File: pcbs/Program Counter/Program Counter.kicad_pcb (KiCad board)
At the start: 2 copper layers, 12 parts, among them J1001 Conn_02x20_Odd_Even, J1002 Conn_02x20_Odd_Even, U2001 74HC245, U2002 74HC245, U3001 74HC245, U3002 74HC245, U4001 74HC245, U4002 74HC245, U5001 74HC245, U5002 74HC245

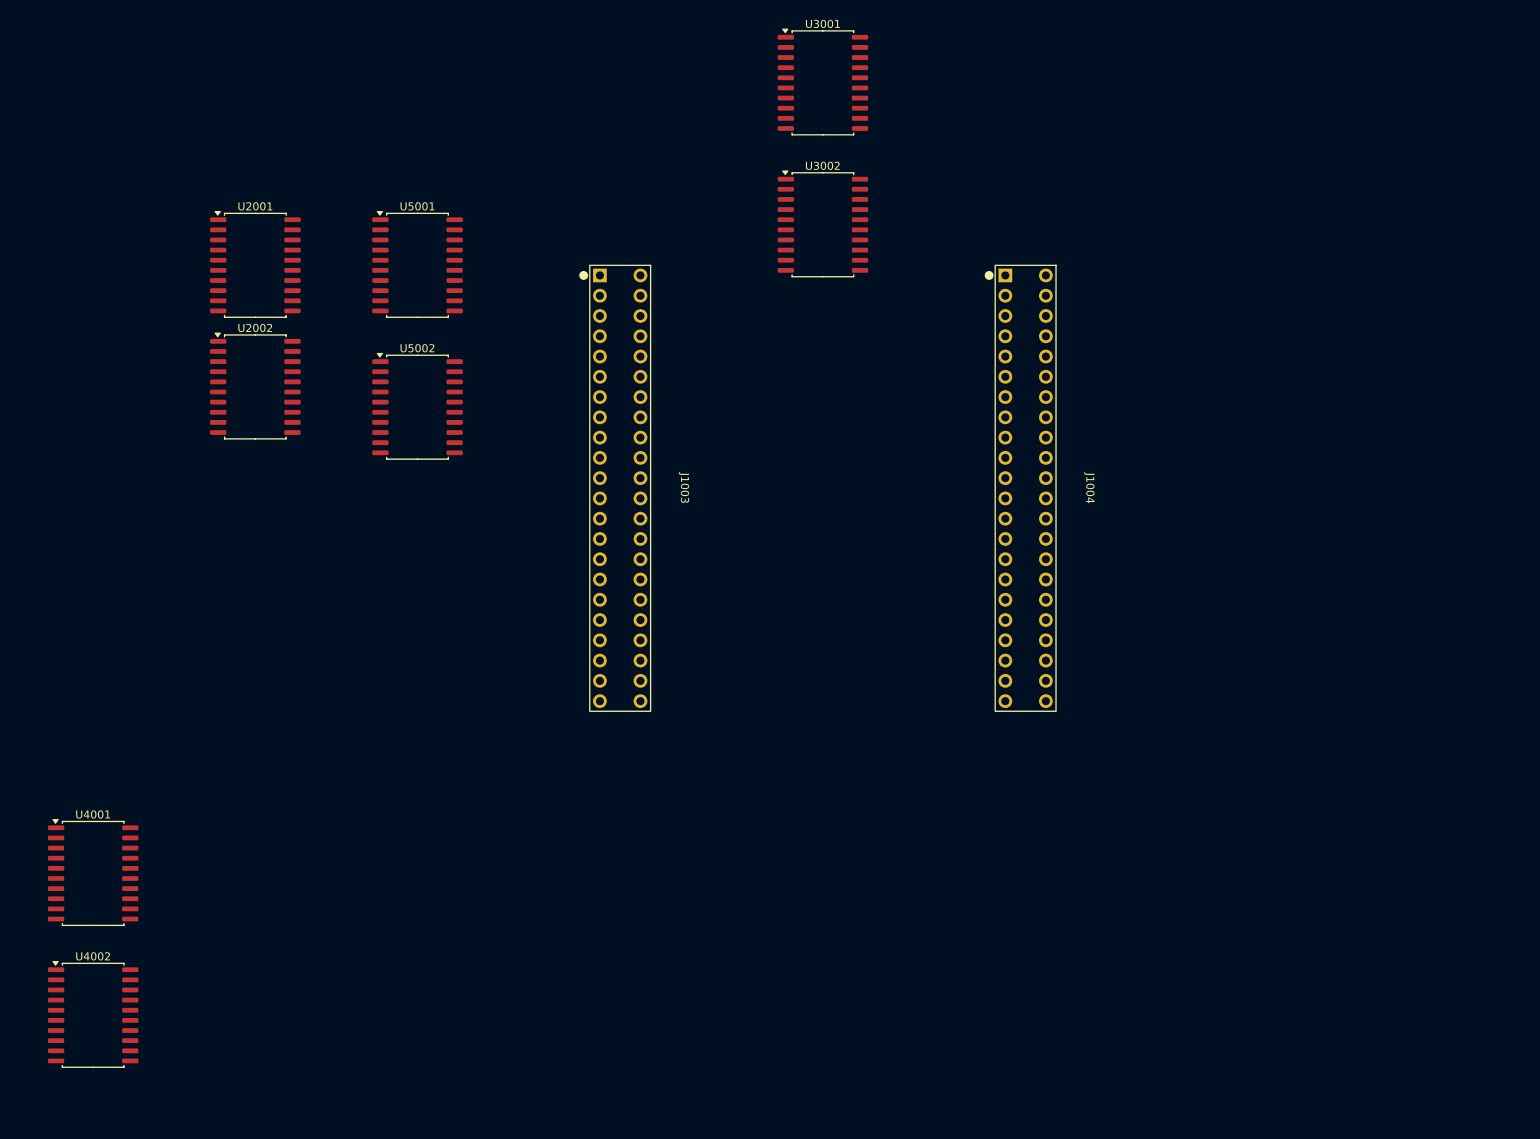
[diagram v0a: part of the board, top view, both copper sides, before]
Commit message: Some preliminary routing
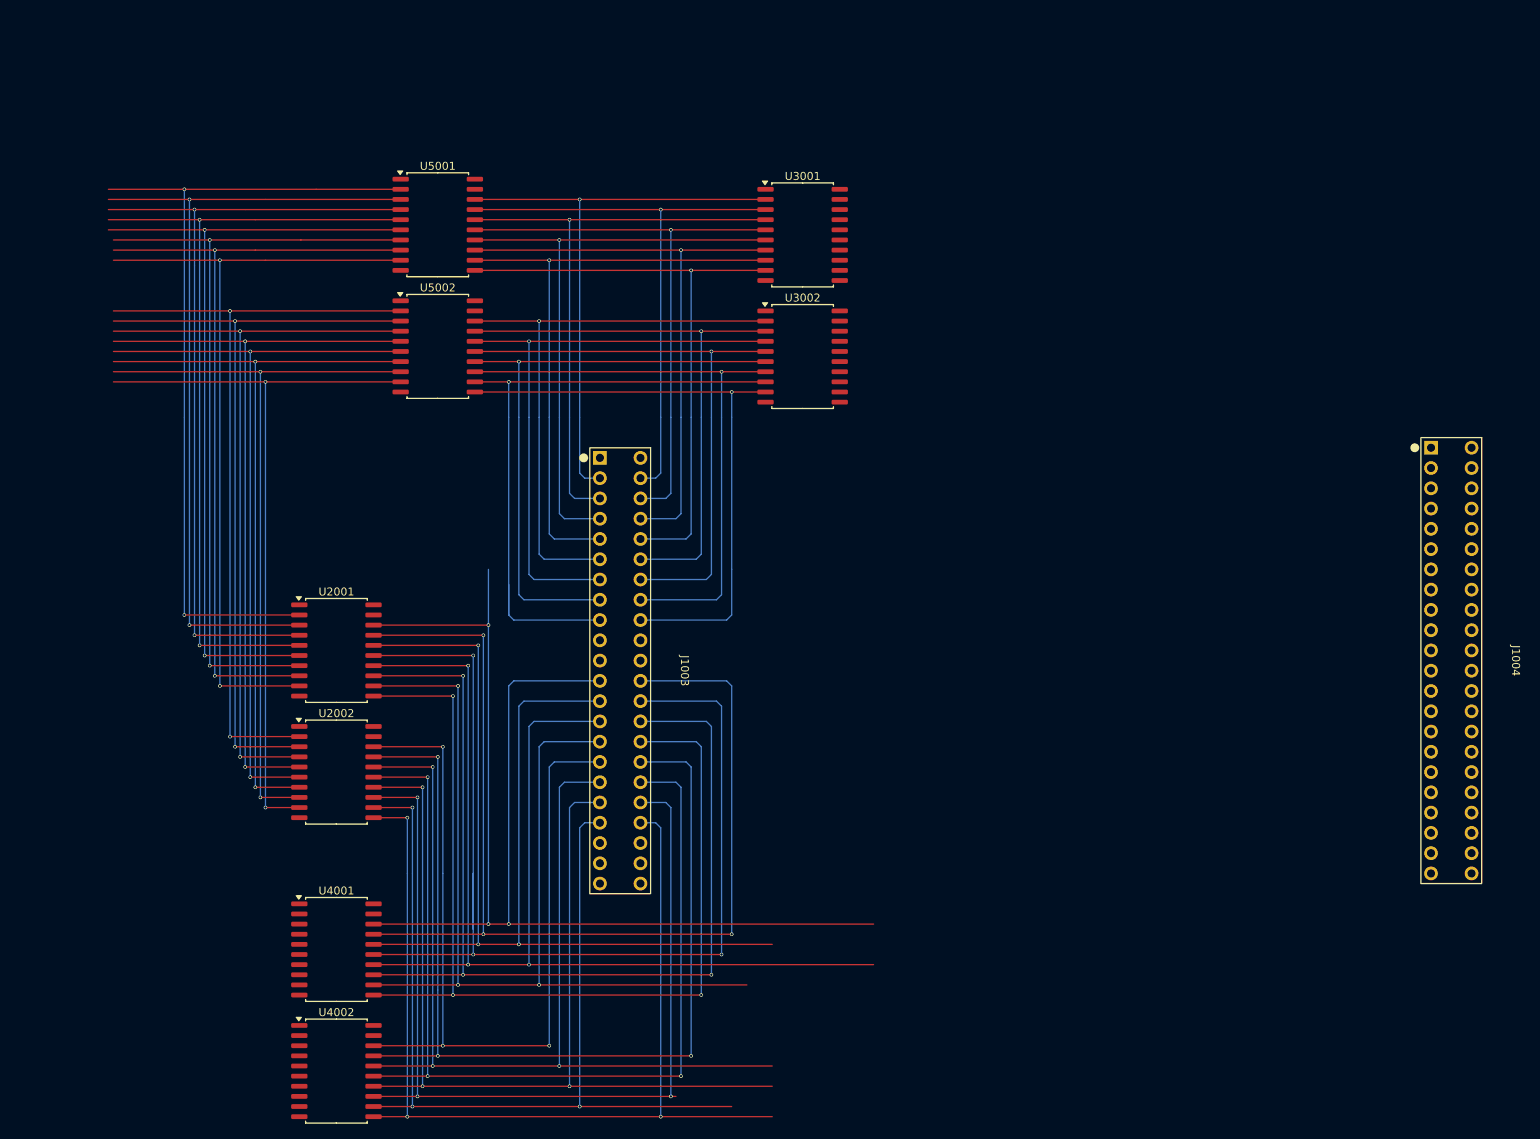
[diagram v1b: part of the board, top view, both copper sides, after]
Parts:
- moved J1004 57.5 mm to (231.1, 100.3)
- moved U2001 49.3 mm to (91.4, 99.1)
- moved U2002 49.3 mm to (91.4, 114.3)
- moved U4001 31.9 mm to (91.4, 136.5)
- moved U4002 31.3 mm to (91.4, 151.8)
- moved J1003 22.9 mm to (127.0, 101.6)
- moved U3001 19.2 mm to (149.9, 47.0)
- moved U3002 16.7 mm to (149.9, 62.2)
- moved U5002 8.03 mm to (104.1, 61.0)
- moved U5001 5.68 mm to (104.1, 45.7)
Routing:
- net /PC.Out0: track 0.00 -> 163.0 mm, vias 0 -> 3
- net /PC.Out4: track 0.00 -> 151.0 mm, vias 0 -> 3
- net /PC.Out3: track 0.00 -> 149.1 mm, vias 0 -> 3
- net /PC.Out2: track 0.00 -> 140.8 mm, vias 0 -> 3
- net /PC.Out1: track 0.00 -> 138.9 mm, vias 0 -> 3
- net /PC.Out10: track 0.00 -> 135.1 mm, vias 0 -> 3
- net /PC.Out6: track 0.00 -> 132.6 mm, vias 0 -> 3
- net /PC.Out12: track 0.00 -> 132.6 mm, vias 0 -> 3
- net /PC.Out5: track 0.00 -> 131.3 mm, vias 0 -> 3
- net /PC.Out15: track 0.00 -> 130.7 mm, vias 0 -> 3
- net /PC.Out9: track 0.00 -> 128.1 mm, vias 0 -> 3
- net /PC.Out7: track 0.00 -> 127.5 mm, vias 0 -> 3
- net /PC.Out14: track 0.00 -> 124.9 mm, vias 0 -> 3
- net /PC.Out11: track 0.00 -> 124.3 mm, vias 0 -> 3
- net /PC.Out13: track 0.00 -> 121.1 mm, vias 0 -> 3
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
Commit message: Thinking about more circuitry
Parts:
- added C6001: 100n, Capacitor_SMD:C_0603_1608Metric, F.Cu at (93.6, 191.5)
- added D6001: Blue, LED_SMD:LED_0603_1608Metric, F.Cu at (112.4, 184.2)
- added D6002: Blue, LED_SMD:LED_0603_1608Metric, F.Cu at (114.3, 198.2)
- added D6003: Blue, LED_SMD:LED_0603_1608Metric, F.Cu at (114.3, 200.8)
- added D6004: Blue, LED_SMD:LED_0603_1608Metric, F.Cu at (114.3, 203.3)
- added D6005: Blue, LED_SMD:LED_0603_1608Metric, F.Cu at (114.3, 205.9)
- added D6006: Blue, LED_SMD:LED_0603_1608Metric, F.Cu at (114.3, 208.5)
- added D6007: Blue, LED_SMD:LED_0603_1608Metric, F.Cu at (114.3, 211.1)
- added D6008: Blue, LED_SMD:LED_0603_1608Metric, F.Cu at (114.3, 213.7)
- added D6009: Blue, LED_SMD:LED_0603_1608Metric, F.Cu at (114.3, 216.3)
- added R6001: 4k7, Resistor_SMD:R_0603_1608Metric, F.Cu at (108.6, 184.2)
- added R6002: 4k7, Resistor_SMD:R_0603_1608Metric, F.Cu at (109.2, 198.1)
- added R6003: 4k7, Resistor_SMD:R_0603_1608Metric, F.Cu at (109.2, 201.3)
- added R6004: 4k7, Resistor_SMD:R_0603_1608Metric, F.Cu at (109.2, 205.1)
- added R6005: 4k7, Resistor_SMD:R_0603_1608Metric, F.Cu at (109.2, 208.3)
- added R6006: 4k7, Resistor_SMD:R_0603_1608Metric, F.Cu at (109.2, 212.1)
- added R6007: 4k7, Resistor_SMD:R_0603_1608Metric, F.Cu at (109.2, 214.6)
- added R6008: 4k7, Resistor_SMD:R_0603_1608Metric, F.Cu at (109.2, 218.5)
- added R6009: 4k7, Resistor_SMD:R_0603_1608Metric, F.Cu at (109.2, 221.0)
- added U6001: 74HC14, Package_SO:SOIC-14_3.9x8.7mm_P1.27mm, F.Cu at (79.4, 184.8)
- added U6002: 74HC08, Package_SO:SOIC-14_3.9x8.7mm_P1.27mm, F.Cu at (88.5, 185.2)
- added U6003: 74HC08, Package_SO:SOIC-14_3.9x8.7mm_P1.27mm, F.Cu at (96.9, 185.2)
- added U6004: 74HC138, Package_DIP:DIP-16_W7.62mm_Socket, F.Cu at (81.9, 192.4)
- moved J1002 9.52 mm to (38.1, 116.2)
- moved J1001 1.91 mm to (38.1, 40.0)

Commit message: More schematic, more layout
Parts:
- added D7001: 1N4148W, Diode_SMD:D_SOD-323, F.Cu at (33.7, 62.9)
- added D7002: 1N4148W, Diode_SMD:D_SOD-323, F.Cu at (45.1, 62.9)
- added D7003: 1N4148W, Diode_SMD:D_SOD-323, F.Cu at (33.7, 65.4)
- added D7004: 1N4148W, Diode_SMD:D_SOD-323, F.Cu at (45.1, 65.4)
- added D7005: 1N4148W, Diode_SMD:D_SOD-323, F.Cu at (33.7, 67.9)
- added D7006: 1N4148W, Diode_SMD:D_SOD-323, F.Cu at (45.1, 67.9)
- added D7007: 1N4148W, Diode_SMD:D_SOD-323, F.Cu at (33.7, 70.5)
- added D7008: 1N4148W, Diode_SMD:D_SOD-323, F.Cu at (45.1, 70.5)
- added D7009: 1N4148W, Diode_SMD:D_SOD-323, F.Cu at (33.7, 73.0)
- added D7010: 1N4148W, Diode_SMD:D_SOD-323, F.Cu at (45.1, 73.0)
- added D7011: 1N4148W, Diode_SMD:D_SOD-323, F.Cu at (33.7, 75.6)
- added D7012: 1N4148W, Diode_SMD:D_SOD-323, F.Cu at (45.1, 75.6)
- added D7013: 1N4148W, Diode_SMD:D_SOD-323, F.Cu at (33.7, 78.1)
- added D7014: 1N4148W, Diode_SMD:D_SOD-323, F.Cu at (45.1, 78.1)
- added D7015: 1N4148W, Diode_SMD:D_SOD-323, F.Cu at (33.7, 80.6)
- added D7016: 1N4148W, Diode_SMD:D_SOD-323, F.Cu at (45.1, 80.6)
- added R7001: 100k, Resistor_SMD:R_0603_1608Metric, F.Cu at (51.4, 80.6)
- added U6005: 74HC14, Package_SO:SOIC-14_3.9x8.7mm_P1.27mm, F.Cu at (69.8, 184.8)
- moved J1004 58.4 mm to (172.7, 101.6)
- moved U4001 1.27 mm to (90.2, 136.5)
- moved U4002 1.27 mm to (90.2, 151.8)
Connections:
- net /Increment Buffer/~{Enable} renamed /~{NormalUpdate}
- J1003 pad B11: /Cycle4 -> /ClockPC
- R6006 pad 2: /Enabler/~{LoadPC} -> /~{LoadPC}
- R6008 pad 2: /Enabler/~{Halt} -> /Increment1
- U2001 pad 19: /Instruction Cycle Buffer/~{Enable} -> /~{InstrCycle}
- U2002 pad 19: /Instruction Cycle Buffer/~{Enable} -> /~{InstrCycle}
- U4001 pad 19: /LoadPC Buffer/~{Enable} -> /~{LoadPC}
- U4002 pad 19: /LoadPC Buffer/~{Enable} -> /~{LoadPC}
- U5001 pad 19: /BranchZero Buffer/~{Enable} -> /~{DoBranch}
- U5002 pad 19: /BranchZero Buffer/~{Enable} -> /~{DoBranch}
- U6002 pad 10: unconnected-(U6002-Pad10) -> GND
- U6002 pad 11: Net-(U6002-Pad11) -> /~{DoBranch}
- U6002 pad 12: unconnected-(U6002-Pad12) -> Net-(U6002-Pad12)
- U6002 pad 13: unconnected-(U6002-Pad13) -> Net-(U6002-Pad13)
- U6002 pad 4: Net-(U6002-Pad11) -> GND
- U6002 pad 5: Net-(U6002-Pad5) -> GND
- U6002 pad 8: Net-(U6002-Pad5) -> unconnected-(U6002-Pad8)
- U6002 pad 9: unconnected-(U6002-Pad9) -> GND
- U6003 pad 3: /Enabler/~{InstrCycle} -> /~{InstrCycle}
- U6003 pad 4: GND -> /Cycle4
- U6003 pad 5: GND -> /Cycle4
- U6003 pad 6: unconnected-(U6003-Pad6) -> /ClockPC
- U6004 pad 11: /Enabler/~{LoadPC} -> /~{LoadPC}
- U6004 pad 9: /Enabler/~{Halt} -> /Increment1
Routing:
- net /~{DoBranch}: track 0.00 -> 123.4 mm, vias 0 -> 2
- net /~{NormalUpdate}: track 0.00 -> 122.1 mm, vias 0 -> 2
- net /PC.Out9: track 128.1 -> 208.6 mm, vias 3 -> 4
- net /PC.Out11: track 124.3 -> 204.8 mm, vias 3 -> 4
- net /PC.Out13: track 121.1 -> 201.0 mm, vias 3 -> 4
- net /PC.Out8: track 109.7 -> 188.3 mm, vias 3 -> 4
- net /PC.Out3: track 149.1 -> 223.8 mm, vias 3 -> 4
- net /PC.Out7: track 127.5 -> 202.3 mm, vias 3 -> 4
- net /PC.Out5: track 131.3 -> 206.1 mm, vias 3 -> 4
- net /PC.Out1: track 138.9 -> 213.7 mm, vias 3 -> 4
- net /Inc.Out15: track 0.00 -> 70.5 mm, vias 0 -> 1
- net /~{InstrCycle}: track 0.00 -> 70.1 mm, vias 0 -> 2
- net /Inc.Out13: track 0.00 -> 68.0 mm, vias 0 -> 1
- net /PC.Out15: track 130.7 -> 197.2 mm, vias 3 -> 4
- net /Inc.Out7: track 0.00 -> 65.5 mm, vias 0 -> 1
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
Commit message: Roughing out the control logic routing
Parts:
- removed the U6002 at (88.5, 185.2)
- added D6010: Blue, LED_SMD:LED_0603_1608Metric, F.Cu at (109.2, 167.6)
- added R6010: 4k7, Resistor_SMD:R_0603_1608Metric, F.Cu at (101.6, 167.6)
- moved U6002 41.8 mm to (55.9, 193.0)
- moved R6008 25.3 mm to (116.8, 194.3)
- moved R6009 25.3 mm to (116.8, 196.8)
- moved U6004 25.3 mm to (101.6, 176.5)
- moved C6001 24.6 mm to (113.0, 176.5)
- moved U6001 24.5 mm to (55.9, 177.8)
- moved R6006 24.1 mm to (116.8, 189.2)
- moved R6007 24.1 mm to (116.8, 191.8)
- moved R6005 22.9 mm to (116.8, 186.7)
- moved R6004 22.3 mm to (116.8, 184.2)
- moved R6003 21.1 mm to (116.8, 181.6)
- moved R6002 20.5 mm to (116.8, 179.1)
- moved D6009 20.5 mm to (120.7, 196.8)
- moved D6008 20.4 mm to (120.7, 194.3)
- moved D6007 20.4 mm to (120.7, 191.8)
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- renumbered U6003 to U6002, U6005 to U6003
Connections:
- U6001 pad 1: /Cycle1 -> /Cycle0
- U6001 pad 11: /Cycle2 -> /Cycle4
- U6001 pad 13: /Cycle4 -> /Cycle3
- U6001 pad 3: GND -> /Cycle1
- U6001 pad 4: unconnected-(U6001-Pad4) -> Net-(U6001-Pad4)
- U6001 pad 5: /Cycle0 -> /Cycle2
- U6001 pad 8: Net-(U6001-Pad8) -> /ClockPC
- U6001 pad 9: /Cycle3 -> Net-(U6001-Pad10)
- U6002 pad 1: Net-(U6001-Pad6) -> Net-(U6001-Pad4)
- U6002 pad 10: Net-(U6001-Pad12) -> Net-(U6001-Pad10)
- U6002 pad 12: Net-(U6001-Pad10) -> Net-(U6001-Pad12)
- U6002 pad 13: Net-(U6001-Pad8) -> Net-(U6001-Pad6)
- U6002 pad 4: /Cycle4 -> Net-(U6002-Pad4)
- U6002 pad 5: /Cycle4 -> Net-(U6002-Pad5)
- U6002 pad 6: /ClockPC -> /~{DoBranch}
- U6003 pad 2: Net-(U6002-Pad13) -> Net-(U6002-Pad4)
- U6003 pad 4: Net-(U6002-Pad12) -> Net-(U6002-Pad5)
- U6003 pad 5: /~{DoBranch} -> GND
- U6003 pad 6: /~{NormalUpdate} -> unconnected-(U6003-Pad6)
- U6003 pad 8: unconnected-(U6005-Pad8) -> /~{NormalUpdate}
- U6003 pad 9: GND -> /~{DoBranch}
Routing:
- net /Increment1: track 0.00 -> 202.1 mm
- net /ClockPC: track 0.00 -> 160.3 mm, vias 0 -> 1
- net /~{InstrCycle}: track 70.1 -> 196.3 mm, vias 2 -> 8
- net /~{DoBranch}: track 123.4 -> 235.3 mm, vias 2 -> 8
- net /~{NormalUpdate}: track 122.1 -> 231.4 mm, vias 2 -> 5
- net /Enabler/~{ExecCycle}: track 0.00 -> 76.6 mm, vias 0 -> 2
- net Net-(U6002-Pad4): track 0.00 -> 58.6 mm, vias 0 -> 4
- net /Enabler/~{BranchZero}: track 0.00 -> 58.1 mm, vias 0 -> 3
- net Net-(U6002-Pad5): track 0.00 -> 49.7 mm, vias 0 -> 4
- net /~{LoadPC}: track 32.6 -> 74.1 mm, vias 2 -> 4
- net /I3: track 0.00 -> 33.0 mm, vias 0 -> 2
- net Net-(U6001-Pad2): track 0.00 -> 30.6 mm, vias 0 -> 2
- net Net-(U6001-Pad12): track 0.00 -> 28.1 mm, vias 0 -> 2
- net Net-(U6001-Pad6): track 0.00 -> 26.6 mm
- net /I2: track 0.00 -> 25.9 mm
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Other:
- board outline added: 172.7 x 185.4 mm
- board text added: "Incrementer"
- board text added: "PC Register"

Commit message: Add JLCJLCJLCJLC to back silkscreen
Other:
- board text added: "JLCJLCJLCJLC"
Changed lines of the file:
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@@
 		(tags "capacitor")
 		(property "Reference" "C6001"
-			(at 0 -1.43 360)
+			(at 0 -1.43 0)
 			(layer "F.SilkS")
 			(effects
@@
 		)
 		(property "Value" "100n"
-			(at 0 1.43 360)
+			(at 0 1.43 0)
 			(layer "F.Fab")
 			(effects
@@
 		)
 		(fp_text user "${REFERENCE}"
-			(at 0 0 360)
+			(at 0 0 0)
 			(layer "F.Fab")
 			(effects
@@
 		(layer "Edge.Cuts")
 	)
+	(gr_text "JLCJLCJLCJLC"
+		(at 35.56 93.98 90)
+		(layer "B.SilkS")
+		(effects
+			(font
+				(size 0.8128 0.8128)
+				(thickness 0.1016)
+			)
+			(justify left bottom mirror)
+		)
+	)
 	(gr_text "Incrementer"

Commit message: Routing.... should be silkscreen and final adjustments next
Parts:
- added D6011: Blue, LED_SMD:LED_0603_1608Metric, F.Cu at (64.8, 190.5)
- added R6011: 4k7, Resistor_SMD:R_0603_1608Metric, F.Cu at (68.6, 190.5)
- moved U6001 5.08 mm to (50.8, 177.8)
- moved U6002 5.08 mm to (50.8, 193.0)
- moved D7001 0.63 mm to (33.0, 62.9)
- moved D7002 0.63 mm to (45.7, 62.9)
- moved D7003 0.63 mm to (33.0, 65.4)
- moved D7004 0.63 mm to (45.7, 65.4)
- moved D7005 0.63 mm to (33.0, 67.9)
- moved D7006 0.63 mm to (45.7, 67.9)
- moved D7007 0.63 mm to (33.0, 70.5)
- moved D7008 0.63 mm to (45.7, 70.5)
- moved D7009 0.63 mm to (33.0, 73.0)
- moved D7010 0.63 mm to (45.7, 73.0)
- moved D7011 0.63 mm to (33.0, 75.6)
- moved D7012 0.63 mm to (45.7, 75.6)
- moved D7013 0.63 mm to (33.0, 78.1)
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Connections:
- net Net-(U6002-Pad4) renamed /Enabler/~{B_{any}}
- J1001 pad 39: /RESET -> /~{RESET}
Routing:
- net /Enabler/B Bus Check/B_{Any}: track 24.2 -> 245.2 mm, vias 1 -> 19
- net /~{RESET}: track 0.00 -> 152.8 mm, vias 0 -> 1
- net /I2: track 25.9 -> 107.1 mm, vias 0 -> 2
- net /I0: track 24.1 -> 105.3 mm, vias 0 -> 2
- net /I3: track 33.0 -> 111.1 mm, vias 2 -> 4
- net /I1: track 24.7 -> 102.8 mm, vias 0 -> 2
- net /C10: track 0.00 -> 70.2 mm, vias 0 -> 2
- net /C14: track 0.00 -> 70.2 mm, vias 0 -> 2
- net /C8: track 0.00 -> 70.2 mm, vias 0 -> 2
- net /C12: track 0.00 -> 70.2 mm, vias 0 -> 2
- net +5V: track 13.6 -> 82.5 mm, vias 8 -> 20
- net /C9: track 0.00 -> 67.1 mm, vias 0 -> 2
- net /C15: track 0.00 -> 67.1 mm, vias 0 -> 2
- net /C13: track 0.00 -> 67.1 mm, vias 0 -> 2
- net /C11: track 0.00 -> 67.1 mm, vias 0 -> 2
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- added copper zone on B.Cu, net +5V
- added copper zone on F.Cu, net GND
